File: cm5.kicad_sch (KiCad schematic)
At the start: 3 parts

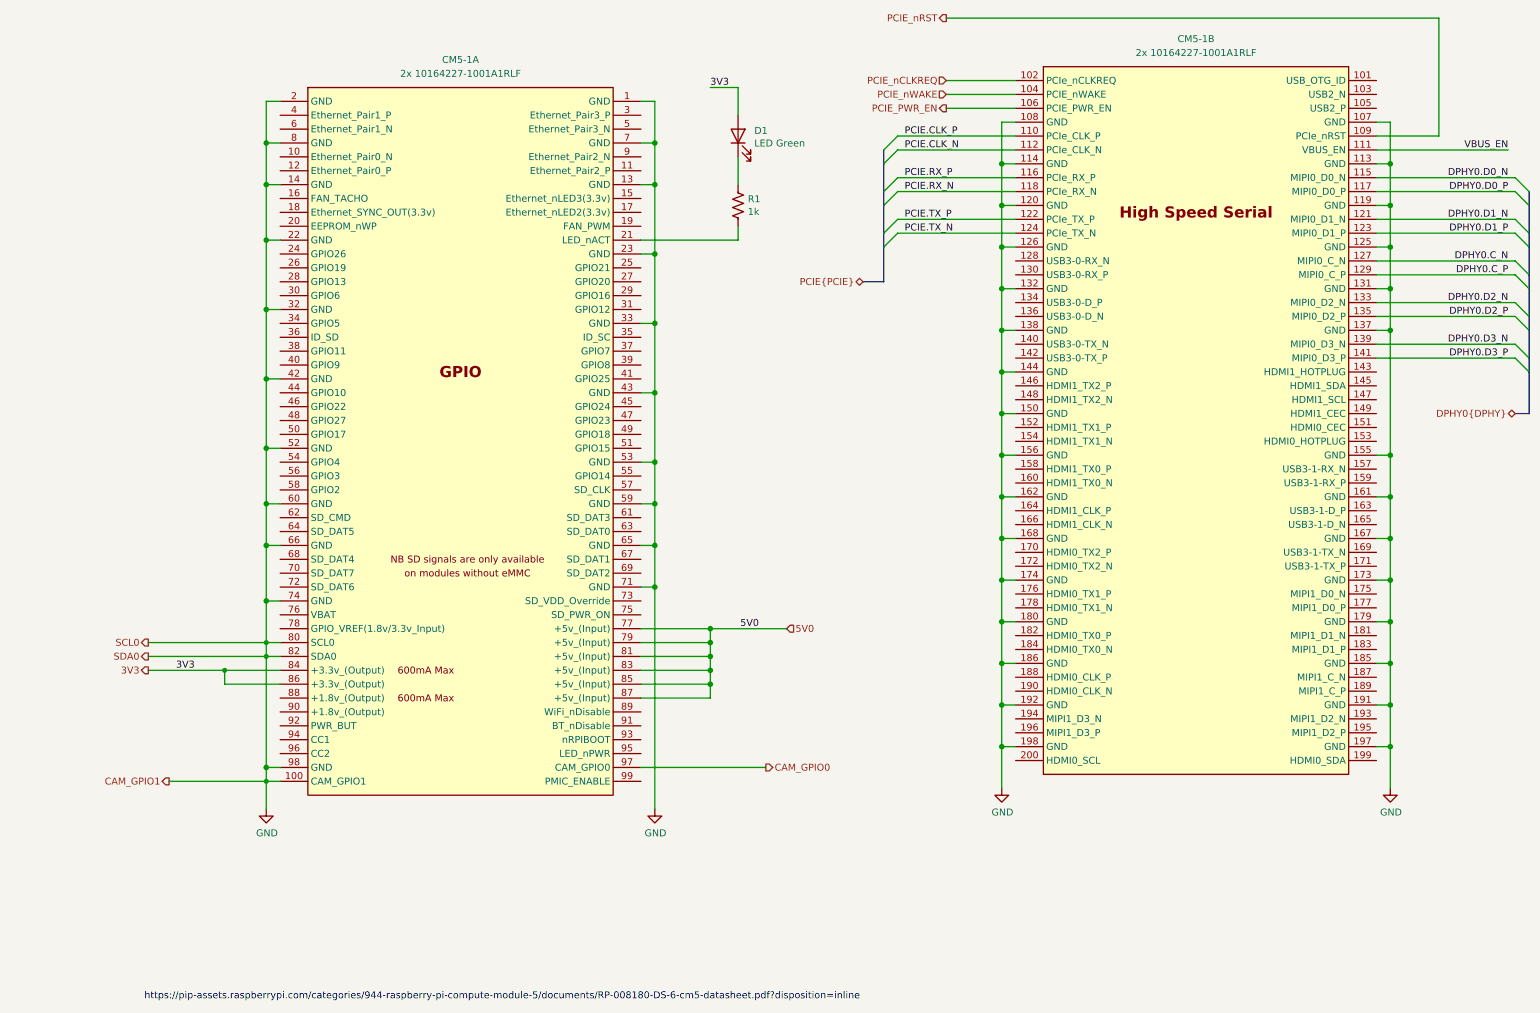
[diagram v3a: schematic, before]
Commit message: added second camera, 6-axis imu
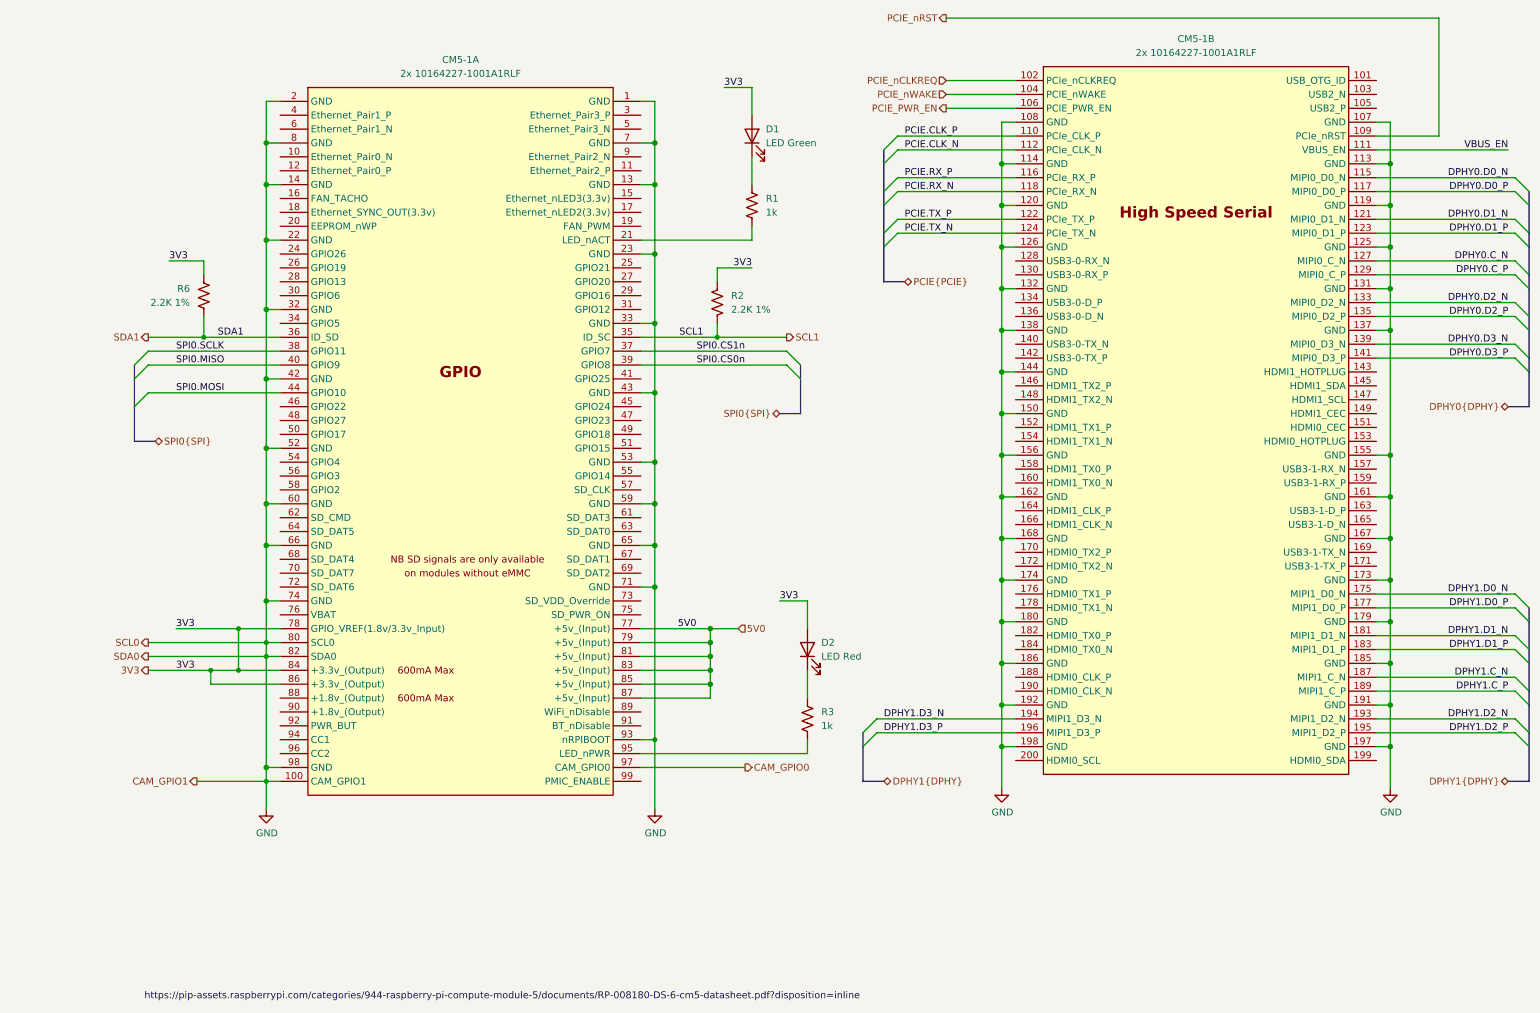
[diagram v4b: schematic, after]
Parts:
- added D2: LED Red, LED_SMD:LED_0603_1608Metric, symbol library:LED
- added R2, R6: 2.2K 1%, Resistor_SMD:R_0402_1005Metric, symbol Device:R_US
- added R3: 1k, Resistor_SMD:R_0402_1005Metric, symbol library:R_US
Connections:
- net 3V3: now also CM5-1.78 (GPIO_VREF(1.8v/3.3v_Input)), D2.2 (A), R2.1, R6.1
- net GND: now also CM5-1.93 (nRPIBOOT)
- net SCL1: now reaches CM5-1.35 (ID_SC)
- net SCL1: now also R2.2
- net SDA1: now reaches CM5-1.36 (ID_SD)
- net SDA1: now also R6.2
- net SPI0.CS1n: now reaches CM5-1.37 (GPIO7)
- net SPI0.SCLK: now reaches CM5-1.38 (GPIO11)
- net SPI0.CS0n: now reaches CM5-1.39 (GPIO8)
- net SPI0.MISO: now reaches CM5-1.40 (GPIO9)
- net SPI0.MOSI: now reaches CM5-1.44 (GPIO10)
- net at CM5-1.95 (LED_nPWR): now also R3.2
- net DPHY1.D0_N: now reaches CM5-1.175 (MIPI1_D0_N)
- net DPHY1.D0_P: now reaches CM5-1.177 (MIPI1_D0_P)
- net DPHY1.D1_N: now reaches CM5-1.181 (MIPI1_D1_N)
- net DPHY1.D1_P: now reaches CM5-1.183 (MIPI1_D1_P)
- net DPHY1.C_N: now reaches CM5-1.187 (MIPI1_C_N)
- net DPHY1.C_P: now reaches CM5-1.189 (MIPI1_C_P)
- net DPHY1.D2_N: now reaches CM5-1.193 (MIPI1_D2_N)
- net DPHY1.D3_N: now reaches CM5-1.194 (MIPI1_D3_N)
- net DPHY1.D2_P: now reaches CM5-1.195 (MIPI1_D2_P)
- net DPHY1.D3_P: now reaches CM5-1.196 (MIPI1_D3_P)
- new net: D2.1 (K), R3.1
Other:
- moved on the sheet: D1, R1

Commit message: annotations, small fixes
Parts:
- renumbered R6 to R2, R2 to R3, R3 to R4
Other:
- moved on the sheet: R2, R3
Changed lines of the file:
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@@
 	)
 	(junction
+		(at 41.91 74.93)
+		(diameter 0)
+		(color 0 0 0 0)
+	)
+	(junction
 		(at 119.38 97.79)
 		(diameter 1.016)
@@
 	)
 	(junction
-		(at 36.83 74.93)
-		(diameter 0)
-		(color 0 0 0 0)
-	)
-	(junction
 		(at 48.26 130.81)
 		(diameter 0)
@@
 	)
 	(junction
+		(at 125.73 74.93)
+		(diameter 0)
+		(color 0 0 0 0)
+	)
+	(junction
 		(at 254 73.66)
 		(diameter 1.016)
@@
 	)
 	(junction
-		(at 130.81 74.93)
-		(diameter 0)
-		(color 0 0 0 0)
-	)
-	(junction
 		(at 38.1 135.89)
 		(diameter 0)
@@
 	(wire
 		(pts
-			(xy 36.83 71.12) (xy 36.83 74.93)
+			(xy 41.91 71.12) (xy 41.91 74.93)
 		)
 		(stroke
@@
 	(wire
 		(pts
-			(xy 116.84 74.93) (xy 130.81 74.93)
+			(xy 116.84 74.93) (xy 125.73 74.93)
 		)
 		(stroke
@@
 	(wire
 		(pts
-			(xy 30.48 60.96) (xy 36.83 60.96)
+			(xy 35.56 60.96) (xy 41.91 60.96)
 		)
 		(stroke
@@
 	(wire
 		(pts
-			(xy 137.16 62.23) (xy 130.81 62.23)
+			(xy 41.91 74.93) (xy 50.8 74.93)
+		)
+		(stroke
+			(width 0)
+			(type solid)
+		)
+	)
+	(wire
+		(pts
+			(xy 132.08 62.23) (xy 125.73 62.23)
 		)
 		(stroke
@@
 	(wire
 		(pts
-			(xy 130.81 72.39) (xy 130.81 74.93)
+			(xy 125.73 72.39) (xy 125.73 74.93)
 		)
 		(stroke
@@
 	(wire
 		(pts
-			(xy 26.67 74.93) (xy 36.83 74.93)
+			(xy 26.67 74.93) (xy 41.91 74.93)
 		)
 		(stroke
@@
 	(wire
 		(pts
-			(xy 130.81 62.23) (xy 130.81 64.77)
+			(xy 125.73 62.23) (xy 125.73 64.77)
 		)
 		(stroke
@@
 	(wire
 		(pts
+			(xy 125.73 74.93) (xy 143.51 74.93)
+		)
+		(stroke
+			(width 0)
+			(type default)
+		)
+	)
+	(wire
+		(pts
 			(xy 48.26 69.85) (xy 48.26 82.55)
 		)
@@
 	(wire
 		(pts
-			(xy 130.81 74.93) (xy 143.51 74.93)
-		)
-		(stroke
-			(width 0)
-			(type default)
-		)
-	)
-	(wire
-		(pts
 			(xy 116.84 97.79) (xy 119.38 97.79)
 		)
@@
 	(wire
 		(pts
-			(xy 36.83 74.93) (xy 50.8 74.93)
-		)
-		(stroke
-			(width 0)
-			(type solid)
-		)
-	)
-	(wire
-		(pts
 			(xy 147.32 123.19) (xy 147.32 128.27)
 		)
@@
 	(wire
 		(pts
-			(xy 36.83 60.96) (xy 36.83 63.5)
+			(xy 41.91 60.96) (xy 41.91 63.5)
 		)
 		(stroke
@@
 	)
 	(label "SCL1"
-		(at 128.27 74.93 180)
+		(at 135.89 74.93 180)
 		(effects
 			(font
@@
 	)
 	(label "3V3"
-		(at 30.48 60.96 0)
+		(at 35.56 60.96 0)
 		(effects
 			(font
@@
 	)
 	(label "3V3"
-		(at 137.16 62.23 180)
+		(at 132.08 62.23 180)
 		(effects
 			(font
@@
 	)
 	(label "SDA1"
-		(at 39.37 74.93 0)
+		(at 31.75 74.93 0)
 		(effects
 			(font
@@
 		(on_board yes)
 		(dnp no)
-		(property "Reference" "#PWR0102"
+		(property "Reference" "#PWR02"
 			(at 254 163.83 0)
 			(effects
@@
 			(project "CUTIE-CITRUS"
 				(path "/40af415e-5e3a-41a5-ab07-08c2181863e4/0ab77a57-2cdd-42e3-9db1-21e8f0163da9"
-					(reference "#PWR0102")
+					(reference "#PWR02")
 					(unit 1)
 				)
@@
 		(on_board yes)
 		(dnp no)
-		(property "Reference" "#PWR0101"
+		(property "Reference" "#PWR01"
 			(at 182.88 163.83 0)
 			(effects
@@
 			(project "CUTIE-CITRUS"
 				(path "/40af415e-5e3a-41a5-ab07-08c2181863e4/0ab77a57-2cdd-42e3-9db1-21e8f0163da9"
-					(reference "#PWR0101")
+					(reference "#PWR01")
 					(unit 1)
 				)
@@
 	(symbol
 		(lib_id "Device:R_US")
-		(at 36.83 67.31 0)
+		(at 41.91 67.31 0)
 		(unit 1)
 		(exclude_from_sim no)
@@
 		(on_board yes)
 		(dnp no)
-		(property "Reference" "R6"
-			(at 34.29 66.04 0)
+		(property "Reference" "R2"
+			(at 39.37 66.04 0)
 			(effects
 				(font
@@
 		)
 		(property "Value" "2.2K 1%"
-			(at 34.29 68.58 0)
+			(at 39.37 68.58 0)
 			(effects
 				(font
@@
 		)
 		(property "Footprint" "Resistor_SMD:R_0402_1005Metric"
-			(at 35.052 67.31 90)
+			(at 40.132 67.31 90)
 			(effects
 				(font
@@
 		)
 		(property "Datasheet" "https://fscdn.rohm.com/en/products/databook/datasheet/passive/resistor/chip_resistor/mcr-e.pdf"
-			(at 36.83 67.31 0)
+			(at 41.91 67.31 0)
 			(effects
 				(font
@@
 		)
 		(property "Description" ""
-			(at 36.83 67.31 0)
+			(at 41.91 67.31 0)
 			(effects
 				(font
@@
 		)
 		(property "Field4" "Farnell"
-			(at 36.83 67.31 0)
+			(at 41.91 67.31 0)
 			(effects
 				(font
@@
 		)
 		(property "Field5" ""
-			(at 36.83 67.31 0)
+			(at 41.91 67.31 0)
 			(effects
 				(font
@@
 		)
 		(property "Field7" ""
-			(at 36.83 67.31 0)
+			(at 41.91 67.31 0)
 			(effects
 				(font
@@
 		)
 		(property "Field6" ""
-			(at 36.83 67.31 0)
+			(at 41.91 67.31 0)
 			(effects
 				(font
@@
 		)
 		(property "Part Description" "Resistor 2.2K M1005 1% 63mW"
-			(at 36.83 67.31 0)
+			(at 41.91 67.31 0)
 			(effects
 				(font
@@
 		)
 		(property "Field8" ""
-			(at 36.83 67.31 0)
+			(at 41.91 67.31 0)
 			(effects
 				(font
@@
 			(project "CUTIE-CITRUS"
 				(path "/40af415e-5e3a-41a5-ab07-08c2181863e4/0ab77a57-2cdd-42e3-9db1-21e8f0163da9"
-					(reference "R6")
+					(reference "R2")
 					(unit 1)
 				)
@@
 	(symbol
 		(lib_id "Device:R_US")
-		(at 130.81 68.58 0)
+		(at 125.73 68.58 0)
 		(mirror y)
 		(unit 1)
@@
 		(on_board yes)
 		(dnp no)
-		(property "Reference" "R2"
-			(at 133.35 67.31 0)
+		(property "Reference" "R3"
+			(at 128.27 67.31 0)
 			(effects
 				(font
@@
 		)
 		(property "Value" "2.2K 1%"
-			(at 133.35 69.85 0)
+			(at 128.27 69.85 0)
 			(effects
 				(font
@@
 		)
 		(property "Footprint" "Resistor_SMD:R_0402_1005Metric"
-			(at 132.588 68.58 90)
+			(at 127.508 68.58 90)
 			(effects
 				(font
@@
 		)
 		(property "Datasheet" "https://fscdn.rohm.com/en/products/databook/datasheet/passive/resistor/chip_resistor/mcr-e.pdf"
-			(at 130.81 68.58 0)
+			(at 125.73 68.58 0)
 			(effects
 				(font
@@
 		)
 		(property "Description" ""
-			(at 130.81 68.58 0)
+			(at 125.73 68.58 0)
 			(effects
 				(font
@@
 		)
 		(property "Field4" "Farnell"
-			(at 130.81 68.58 0)
+			(at 125.73 68.58 0)
 			(effects
 				(font
@@
 		)
 		(property "Field5" ""
-			(at 130.81 68.58 0)
+			(at 125.73 68.58 0)
 			(effects
 				(font
@@
 		)
 		(property "Field7" ""
-			(at 130.81 68.58 0)
+			(at 125.73 68.58 0)
 			(effects
 				(font
@@
 		)
 		(property "Field6" ""
-			(at 130.81 68.58 0)
+			(at 125.73 68.58 0)
 			(effects
 				(font
@@
 		)
 		(property "Part Description" "Resistor 2.2K M1005 1% 63mW"
-			(at 130.81 68.58 0)
+			(at 125.73 68.58 0)
 			(effects
 				(font
@@
 		)
 		(property "Field8" ""
-			(at 130.81 68.58 0)
+			(at 125.73 68.58 0)
 			(effects
 				(font
@@
 			(project "CUTIE-CITRUS"
 				(path "/40af415e-5e3a-41a5-ab07-08c2181863e4/0ab77a57-2cdd-42e3-9db1-21e8f0163da9"
-					(reference "R2")
+					(reference "R3")
 					(unit 1)
 				)
@@
 		(on_board yes)
 		(dnp no)
-		(property "Reference" "#PWR01"
+		(property "Reference" "#PWR04"
 			(at 119.38 167.64 0)
 			(effects
@@
 			(project "CUTIE-CITRUS"
 				(path "/40af415e-5e3a-41a5-ab07-08c2181863e4/0ab77a57-2cdd-42e3-9db1-21e8f0163da9"
-					(reference "#PWR01")
+					(reference "#PWR04")
 					(unit 1)
 				)
@@
 		(on_board yes)
 		(dnp no)
-		(property "Reference" "R3"
+		(property "Reference" "R4"
 			(at 149.86 143.51 0)
 			(effects
@@
 			(project "CUTIE-CITRUS"
 				(path "/40af415e-5e3a-41a5-ab07-08c2181863e4/0ab77a57-2cdd-42e3-9db1-21e8f0163da9"
-					(reference "R3")
+					(reference "R4")
 					(unit 1)
 				)
@@
 		(on_board yes)
 		(dnp no)
-		(property "Reference" "#PWR02"
+		(property "Reference" "#PWR03"
 			(at 48.26 167.64 0)
 			(effects
@@
 			(project "CUTIE-CITRUS"
 				(path "/40af415e-5e3a-41a5-ab07-08c2181863e4/0ab77a57-2cdd-42e3-9db1-21e8f0163da9"
-					(reference "#PWR02")
+					(reference "#PWR03")
 					(unit 1)
 				)

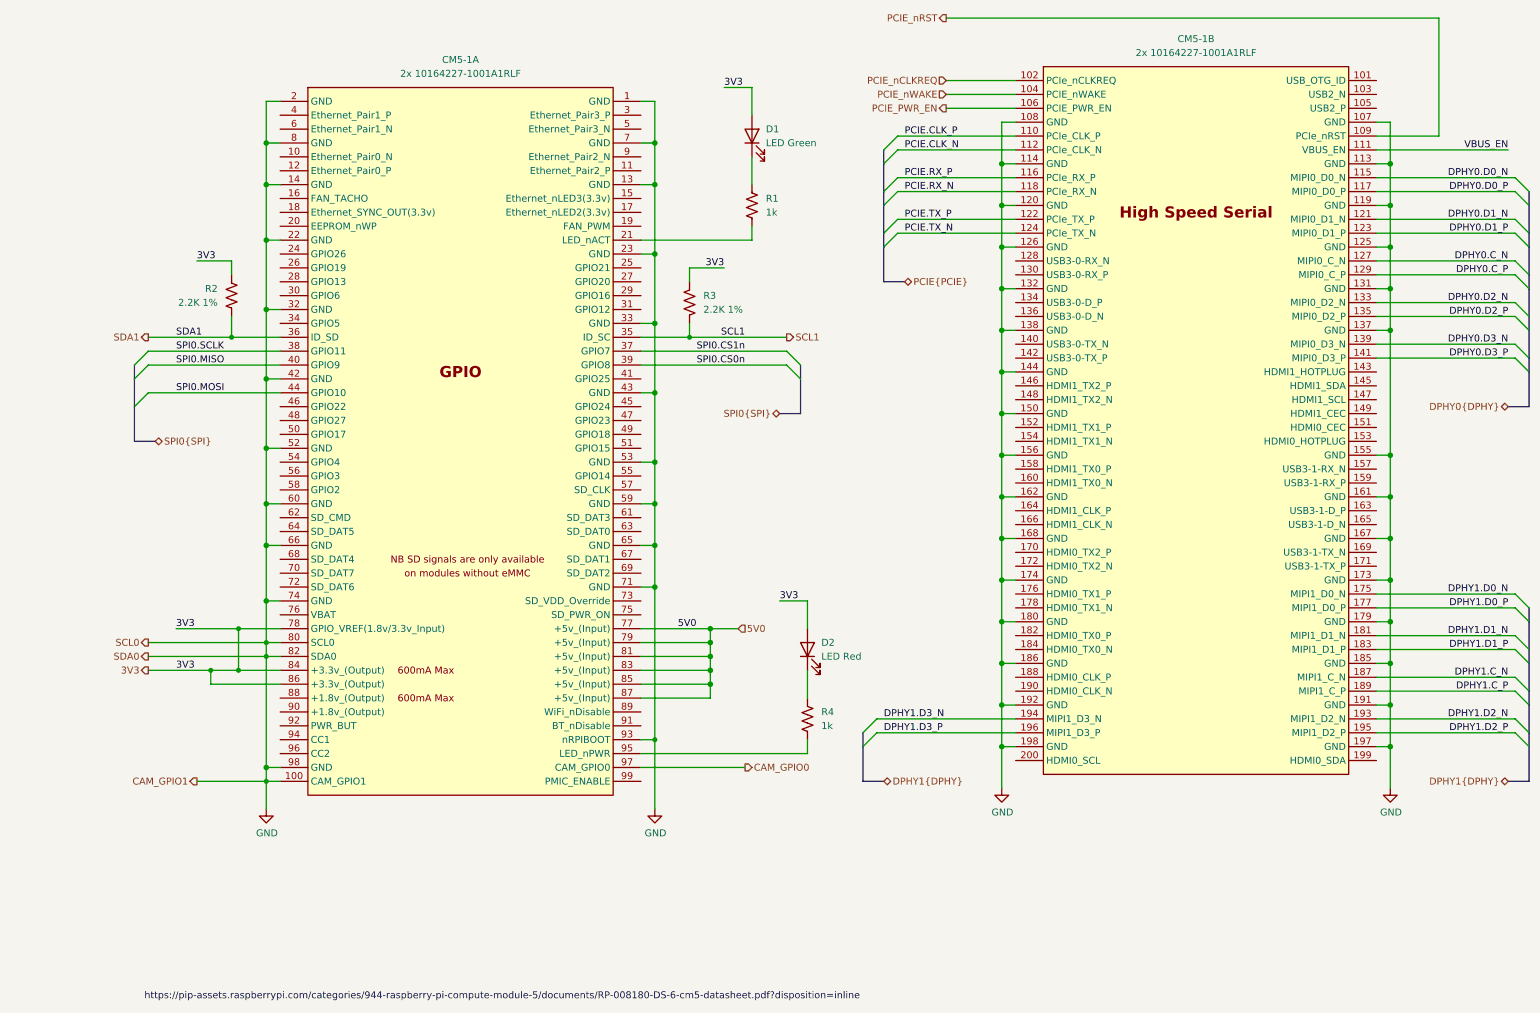
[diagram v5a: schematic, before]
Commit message: extra abstraction layer for cm5 conns.
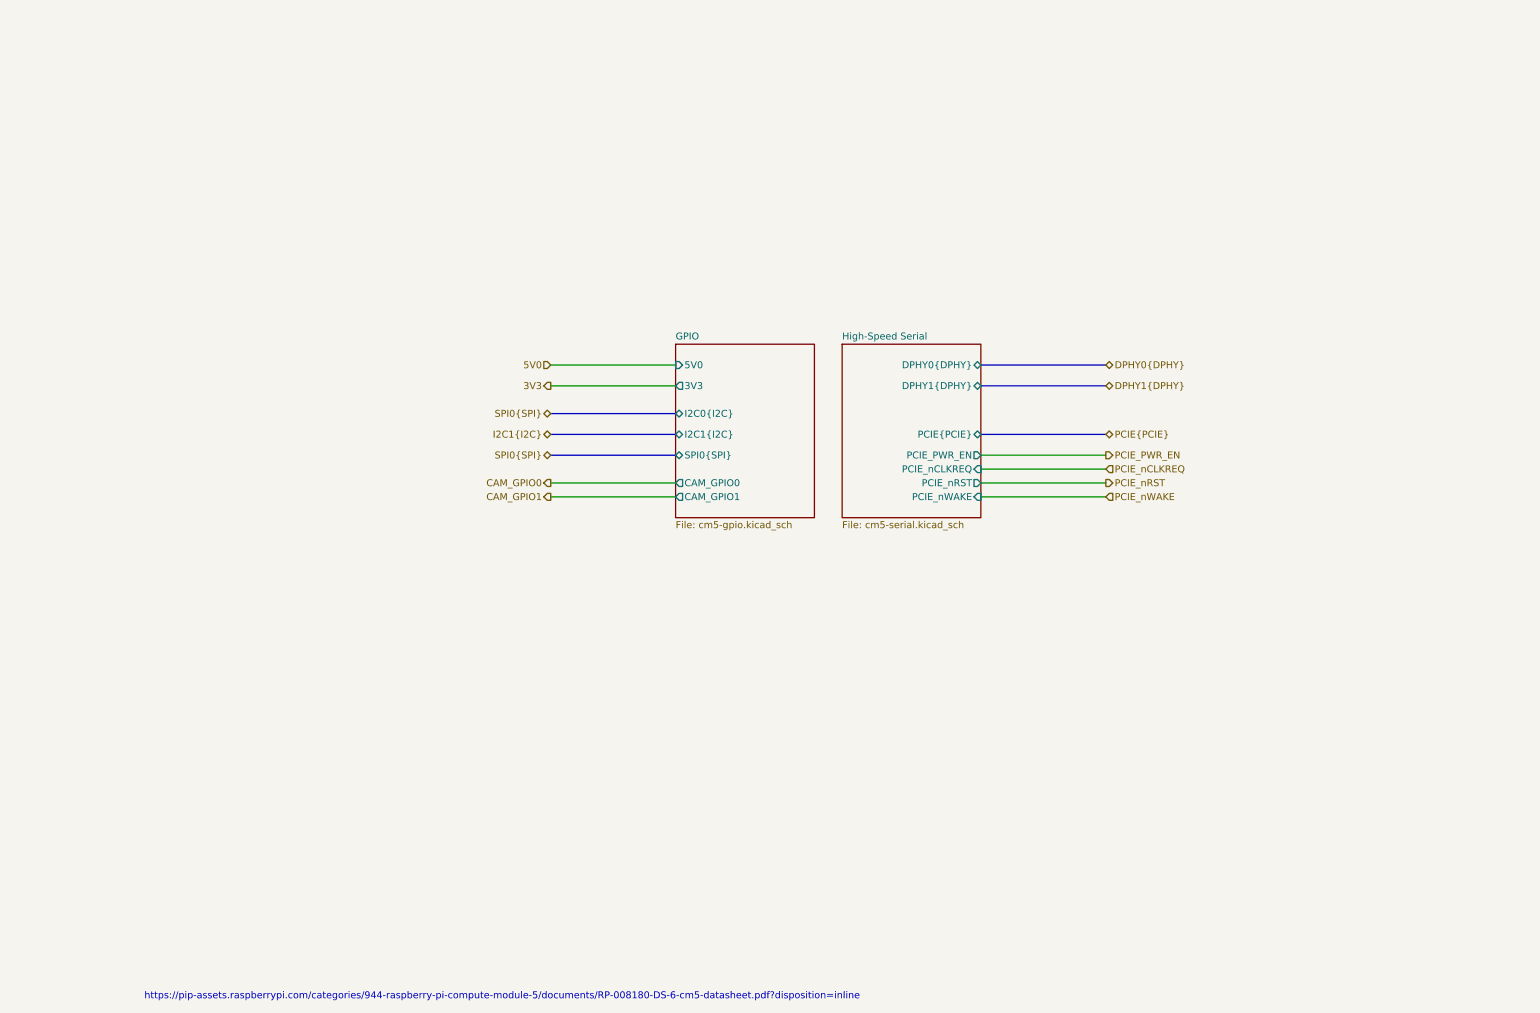
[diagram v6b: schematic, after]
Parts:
- removed CM5-1: 2x 10164227-1001A1RLF, library:RPi-CM5, symbol library:CM5
- removed D1: LED Green, LED_SMD:LED_0603_1608Metric, symbol library:LED
- removed D2: LED Red, LED_SMD:LED_0603_1608Metric, symbol library:LED
- removed R1, R4: 1k, Resistor_SMD:R_0402_1005Metric, symbol library:R_US
- removed R2, R3: 2.2K 1%, Resistor_SMD:R_0402_1005Metric, symbol Device:R_US
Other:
- added sheet GPIO (cm5-gpio.kicad_sch)
- added sheet High-Speed Serial (cm5-serial.kicad_sch)
- company: (none) -> Andre S Winkel | Highlander Space Program | University of California, Riverside
- title: (none) -> CUTIE-CITRUS PCB
